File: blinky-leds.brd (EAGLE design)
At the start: 100 x 80 mm, 14 parts, among them IC1 555, IC2 4017D

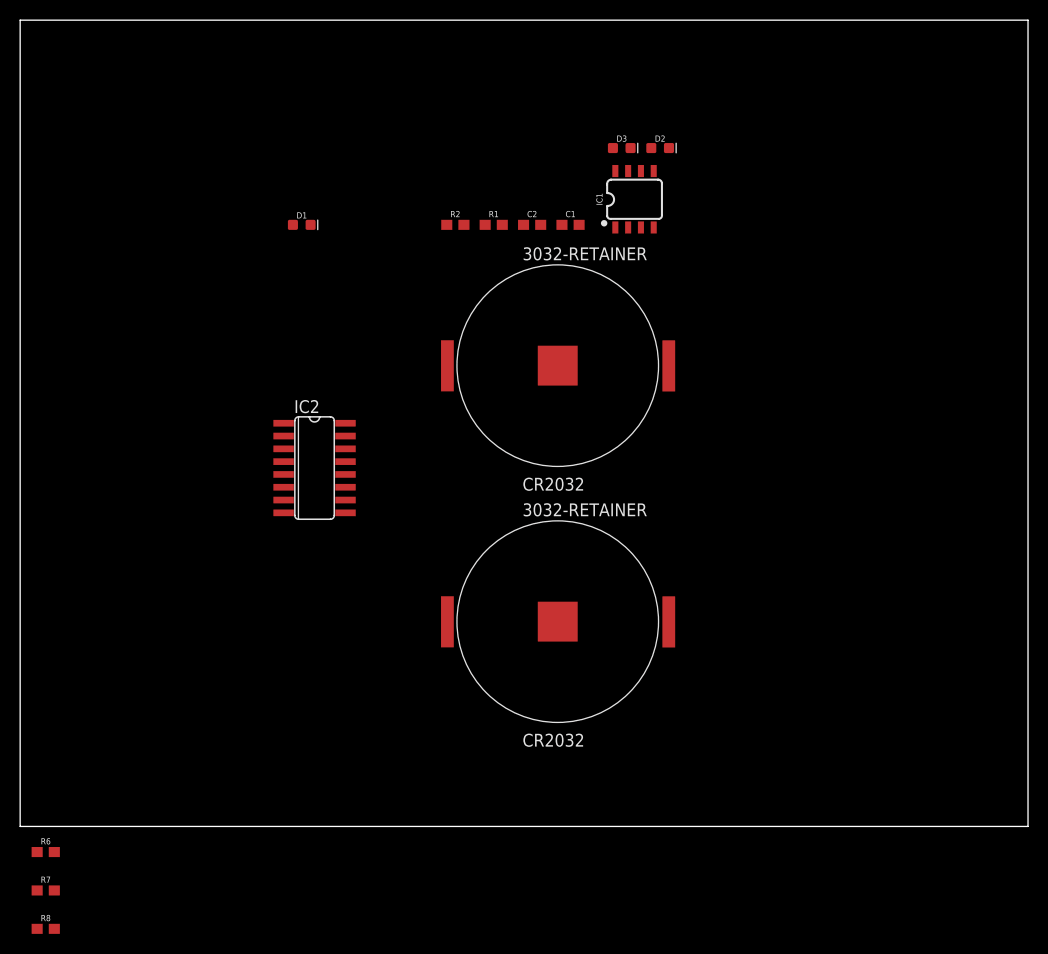
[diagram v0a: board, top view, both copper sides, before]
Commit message: Right schematic
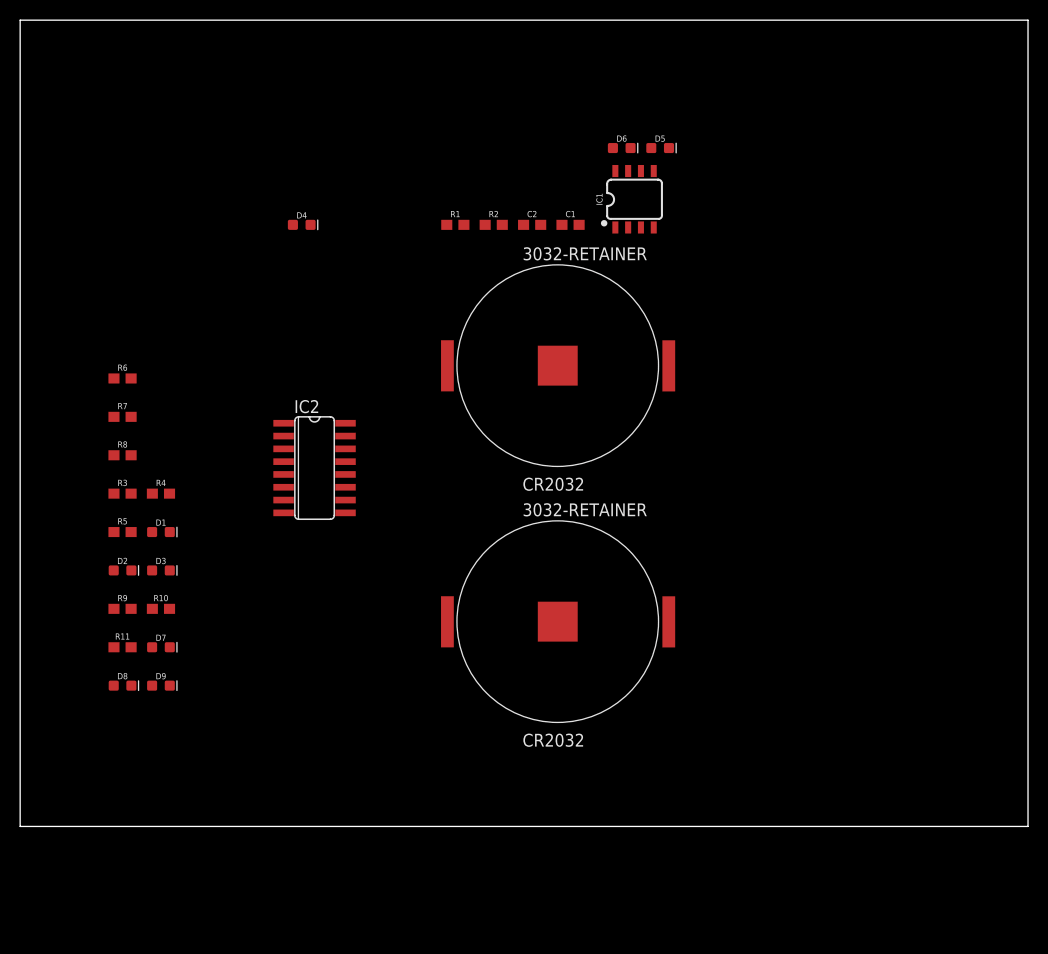
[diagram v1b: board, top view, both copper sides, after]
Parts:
- added D4, D5, D6, D7, D8, D9: (no value), SparkFun-LED:LED-0603
- added R10, R11, R3, R4, R5, R9: 820, SparkFun-Resistors:0603
- R1: value 33k -> 10k
- R2: value 10k -> 33k
- moved D2 67.8 mm to (10.2, 25.4)
- moved D3 62.0 mm to (14.0, 25.4)
- moved R6 47.6 mm to (10.2, 44.5)
- moved R7 47.6 mm to (10.2, 40.6)
- moved R8 47.6 mm to (10.2, 36.8)
- moved D1 33.5 mm to (14.0, 29.2)
- moved BT1 25.4 mm to (53.3, 45.7)
- moved BT2 25.4 mm to (53.3, 20.3)
- moved R1 3.81 mm to (43.2, 59.7)
- moved R2 3.81 mm to (47.0, 59.7)
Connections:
- removed net N$5: D3.A, IC2.4
- new net N$13: D3.C, R5.1
- new net N$14: D2.C, R4.1
- new net N$15: D1.C, R3.1
- new net N$16: D9.C, R11.1
- new net N$17: D8.C, R10.1
- new net N$18: D7.C, R9.1
- new net N$20: D7.A, D8.A, D9.A, IC2.4
- net N$1: now also BT1.P$1, BT2.P$2, BT2.P$3; no longer BT1.P$2, BT1.P$3, BT2.P$1
- net N$11: now also D5.C; no longer D2.C
- net N$12: now also D4.C; no longer D1.C
- net N$2: now also D6.C; no longer D3.C
- net N$3: now also D2.A, D3.A
- net N$4: now also D4.A, D5.A, D6.A; no longer D2.A
- net N$8: now also R1.1, R2.2; no longer R1.2, R2.1
- net N$9: now also R2.1; no longer R1.1
- net VDD: now also BT1.P$2, BT1.P$3, R1.2; no longer BT2.P$2, BT2.P$3, R2.2
- net VSS: now also BT2.P$1, R10.2, R11.2, R3.2, R4.2, R5.2, R9.2; no longer BT1.P$1
